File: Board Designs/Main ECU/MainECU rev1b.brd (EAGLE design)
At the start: 121.2 x 79.8 mm, 145 parts, among them X1 CONNECTOR-37, X2 CONNECTOR-4AUTOSPORT, X3 CONNECTOR-4NANO-FIT-VERTICAL-4, X4 CONNECTOR-4NANO-FIT-VERTICAL-4

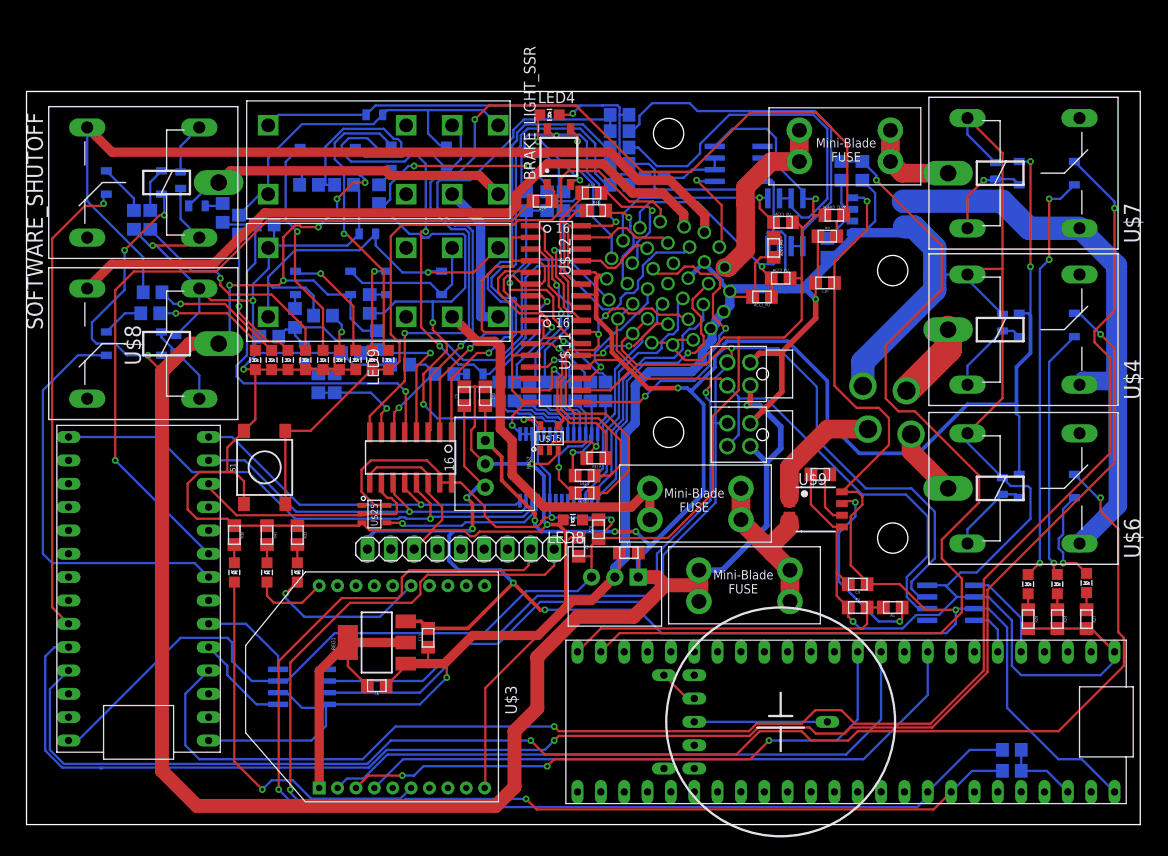
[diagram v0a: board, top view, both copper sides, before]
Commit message: Main ECU rev{1,2}: Update pullup/down resistor informational text, Main ECU rev1b: Update pinout to match Main ECU rev2
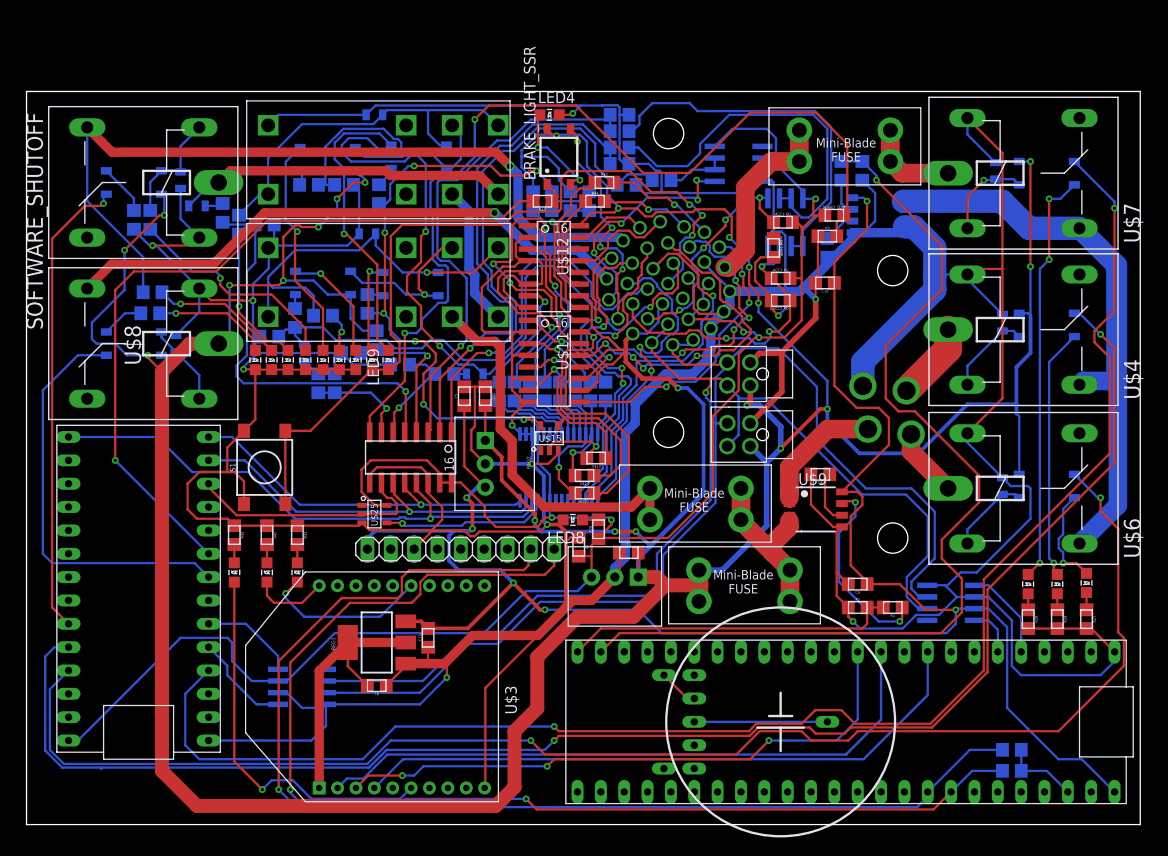
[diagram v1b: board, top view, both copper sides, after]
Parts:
- moved ACC2_PD 2.07 mm to (82.0, 57.0)
- moved R43 1.81 mm to (62.9, 69.8)
- moved R44 1.02 mm to (61.8, 67.8)
- moved BR_FILTR 0.80 mm to (69.1, 70.1)
- moved C12 0.76 mm to (65.3, 69.6)
- moved U$16 0.76 mm to (59.2, 67.8)
- moved U$20 0.76 mm to (61.2, 67.8)
- moved U$21 0.76 mm to (55.1, 67.8)
- moved U$22 0.51 mm to (57.1, 67.8)
- moved IMD_LATCH_SSR 0.40 mm to (41.8, 58.8)
- moved R12 0.25 mm to (37.1, 56.6)
- moved U$11 0.23 mm to (57.4, 50.4)
- moved U$12 0.23 mm to (57.4, 60.7)
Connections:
- net +12V: now also X1.P$10, X1.P$34; no longer X1.P$7
- net +5V: now also X1.P$27, X1.P$28, X1.P$29; no longer X1.P$11, X1.P$12, X1.P$13
- net BMS_OK: now also X1.P$31; no longer X1.P$19
- net BRAKE_LIGHT: now also X1.P$9; no longer X1.P$6
- net CANH: now also X1.P$12, X1.P$13; no longer X1.P$10, X1.P$25
- net CANL: now also X1.P$11, X1.P$26; no longer X1.P$24, X1.P$9
- net DASH_CTRL10: now also X1.P$32; no longer X1.P$28
- net DASH_CTRL11: now also X1.P$6; no longer X1.P$35
- net DASH_CTRL12: now also X1.P$22; no longer X1.P$34
- net DASH_CTRL9: now also X1.P$23; no longer X1.P$29
- net DASH_IO1: now also X1.P$1; no longer X1.P$22
- net DASH_IO2: now also X1.P$2; no longer X1.P$23
- net DASH_IO3: now also X1.P$3; no longer X1.P$21
- net DASH_IO4: now also X1.P$4; no longer X1.P$20
- net DASH_IO5: now also X1.P$18; no longer X1.P$32
- net DASH_IO6: now also X1.P$19; no longer X1.P$33
- net DASH_IO7: now also X1.P$20; no longer X1.P$26
- net DASH_IO8: now also X1.P$21; no longer X1.P$27
- net INVERTER_SUPPLY: now also X1.P$7; no longer X1.P$2
- net LATCH_EXT_BUTTON: now also X1.P$37; no longer X1.P$3
- net OKHS: now also X1.P$33; no longer X1.P$8
- net SHUTDOWN_D: now also X1.P$5; no longer X1.P$1
- net SIGNAL_ACCEL1: now also X1.P$25; no longer X1.P$5
- net SIGNAL_ACCEL2: now also X1.P$24; no longer X1.P$4
- net SIGNAL_BRAKE: now also X1.P$8; no longer X1.P$18
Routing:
- net +12V: track 461.3 -> 487.5 mm, vias 17 -> 22
- net DASH_IO6: track 35.0 -> 61.0 mm, vias 1 -> 5
- net DASH_IO7: track 32.7 -> 57.9 mm, vias 2 -> 4
- net SIGNAL_BRAKE: track 10.5 -> 26.0 mm, vias 1 -> 4
- net +5V: track 299.8 -> 286.8 mm, vias 8 -> 12
- net LATCH_EXT_BUTTON: track 75.0 -> 87.8 mm, vias 0 -> 3
- net DASH_CTRL10: track 28.6 -> 40.7 mm, vias 0 -> 1
- net INVERTER_SUPPLY: track 74.9 -> 62.9 mm, vias 0 -> 1
- net DASH_CTRL12: track 25.1 -> 35.4 mm, vias 0 -> 3
- net BRAKE_LIGHT: track 15.9 -> 25.3 mm, vias 1 -> 4
- net CANH: track 134.2 -> 125.5 mm, vias 1 -> 0
- net OKHS: track 50.5 -> 57.7 mm
- net SHUTDOWN_D: track 93.5 -> 86.6 mm, vias 0 -> 1
- net DASH_CTRL11: track 27.9 -> 34.7 mm, vias 0 -> 1
- net SIGNAL_ACCEL2: track 26.2 -> 32.4 mm, vias 1 -> 3
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
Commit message: Update MainECU rev1b: Update revision silkscreen, Move TLP291-4 (package dimensions incorrect)
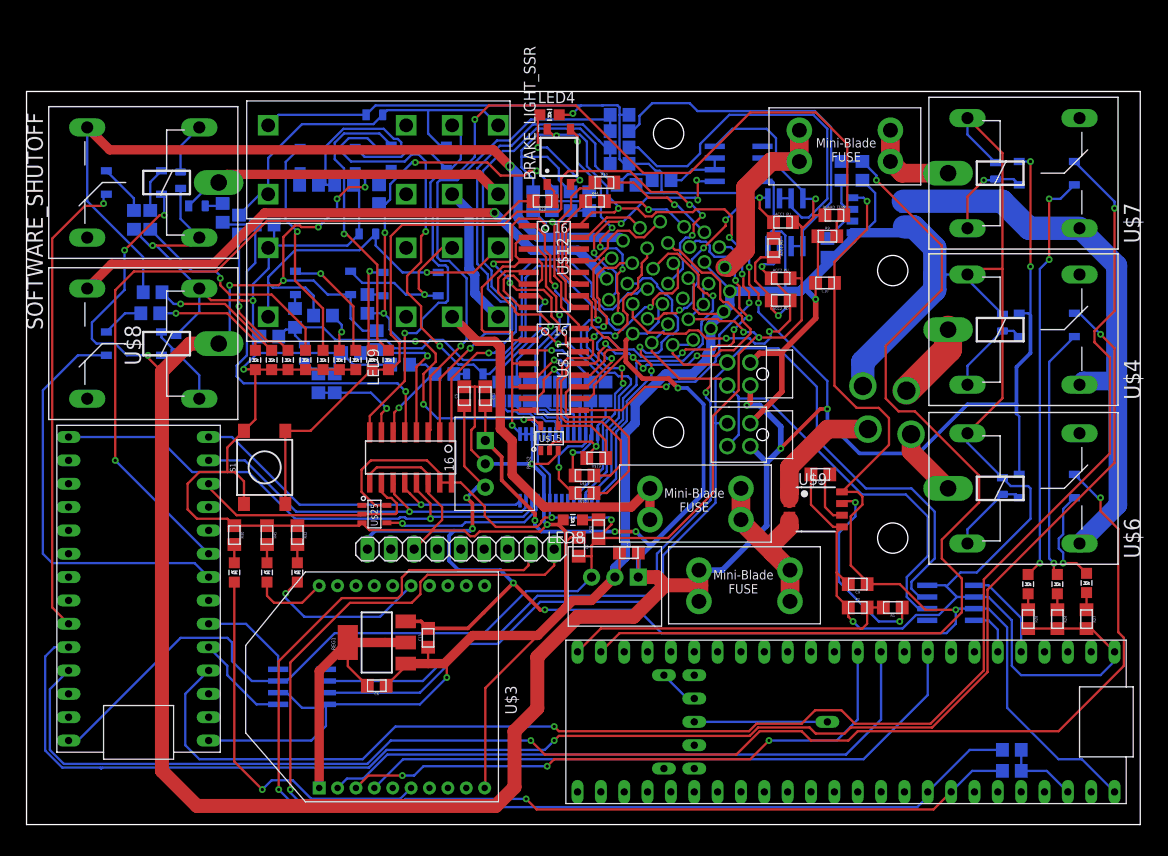
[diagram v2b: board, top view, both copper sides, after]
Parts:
- moved U$11 0.89 mm to (57.4, 49.5)
- flipped U$26 to the bottom, turned to 270 degrees
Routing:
- net +12V: track 487.5 -> 488.8 mm
- net N$55: track 5.39 -> 6.48 mm
- net DASH_IO8: track 37.4 -> 36.4 mm
- net N$62: track 29.5 -> 30.4 mm
- net DASH_IO6: track 61.0 -> 61.7 mm
- net N$61: track 16.7 -> 17.3 mm
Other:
- board text added: "HyTech 2019 Main ECU rev1b"
- board text removed: "HyTech 2019 Main ECU rev1"

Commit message: Library: Update XBee footprint, Add zener diode, toggle TXB010{4,6} value option; MainECU rev1b: add SPI level shifter, switch to separate SPI CS pins, move RTC batt inside board footprint; MainECU rev3: init
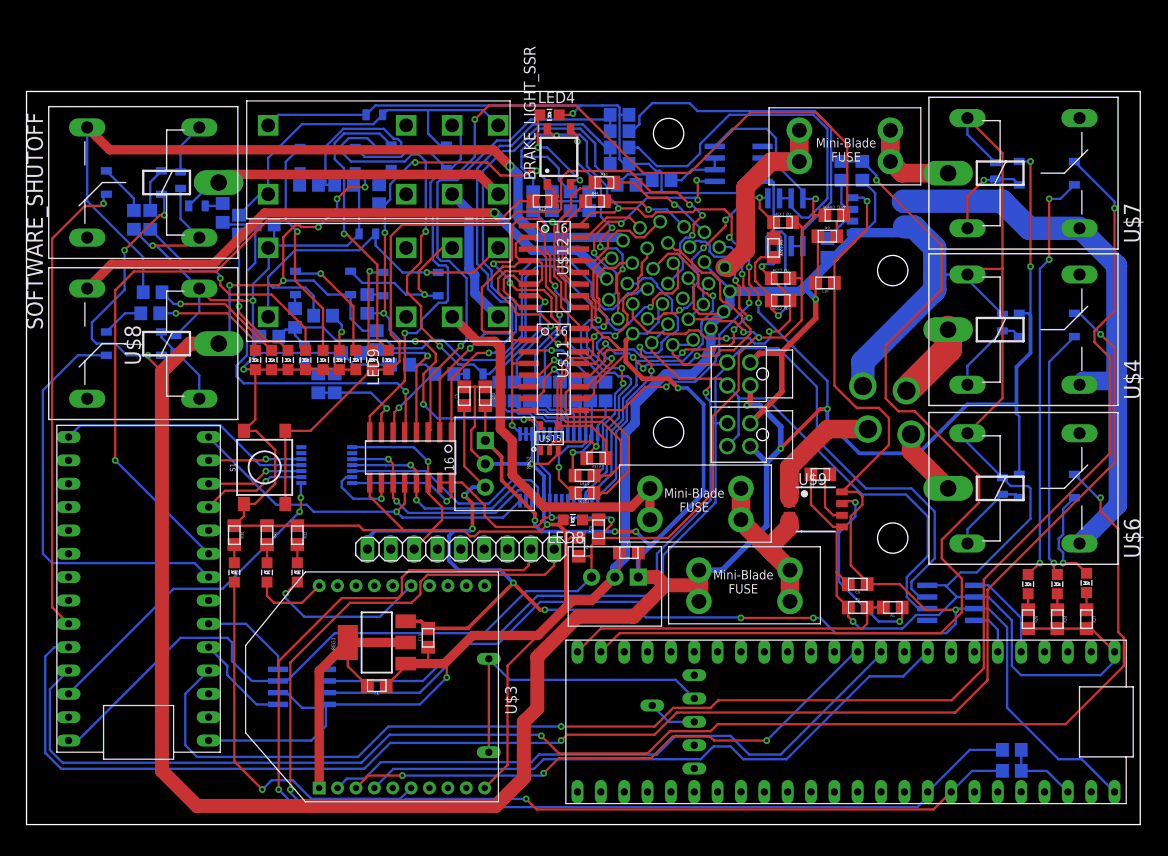
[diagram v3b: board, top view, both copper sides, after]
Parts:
- U$25: value SN74LVC1G06 -> TXB0104TSSOP; device HyTechDevices:SOT-23-5 -> HyTechDevices:TSSOP-14
- moved U$26 19.1 mm to (63.0, 13.0)
- moved U$25 7.54 mm to (32.5, 39.1), flipped to the bottom, turned to 90 degrees
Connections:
- removed net CHIP_SELECT: U$1.D10(TX2), U$18.10, U$25.2
- removed net CHIP_SELECT_INVERTED: U$17.11, U$25.4
- new net 3.3V_MAIN_TEENSY: U$1.3.3V, U$25.1
- new net CS1_5V: U$18.10, U$25.13
- new net CS1_TEENSY: U$1.D9(RX2), U$25.2
- new net CS2_5V: U$17.11, U$25.12
- new net CS2_TEENSY: U$1.D10(TX2), U$25.3
- new net MOSI_5V: U$17.13, U$18.11, U$25.10
- new net N$65: U$25.7
- new net SCK_5V: U$17.12, U$18.13, U$25.11
- net +5V: now also U$25.14; no longer U$25.5
- net GND: now also U$25.8; no longer U$25.3
- net MOSI_TEENSY: now also U$25.5; no longer U$17.13, U$18.11
- net SCK_TEENSY: now also U$25.4; no longer U$17.12, U$18.13
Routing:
- net 3.3V_MAIN_TEENSY: track 0.00 -> 36.5 mm, vias 0 -> 2
- net SCK_TEENSY: track 60.1 -> 27.6 mm, vias 1 -> 0
- net MOSI_TEENSY: track 41.7 -> 10.1 mm
- net N$41: track 4.35 -> 34.3 mm
- net CHIP_SELECT: track 26.4 -> 0.00 mm
- net SCK_5V: track 0.00 -> 25.9 mm, vias 0 -> 2
- net MOSI_5V: track 0.00 -> 25.6 mm, vias 0 -> 2
- net CS2_5V: track 0.00 -> 24.5 mm
- net CHIP_SELECT_INVERTED: track 18.2 -> 0.00 mm, vias 1 -> 0
- net CS1_TEENSY: track 0.00 -> 11.4 mm, vias 0 -> 1
- net CS2_TEENSY: track 0.00 -> 10.7 mm, vias 0 -> 1
- net N$64: track 14.5 -> 5.31 mm
- net CS1_5V: track 0.00 -> 8.56 mm, vias 0 -> 1
- net XBDI: track 65.0 -> 61.1 mm
- net +5V: track 287.1 -> 284.2 mm, vias 12 -> 13
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
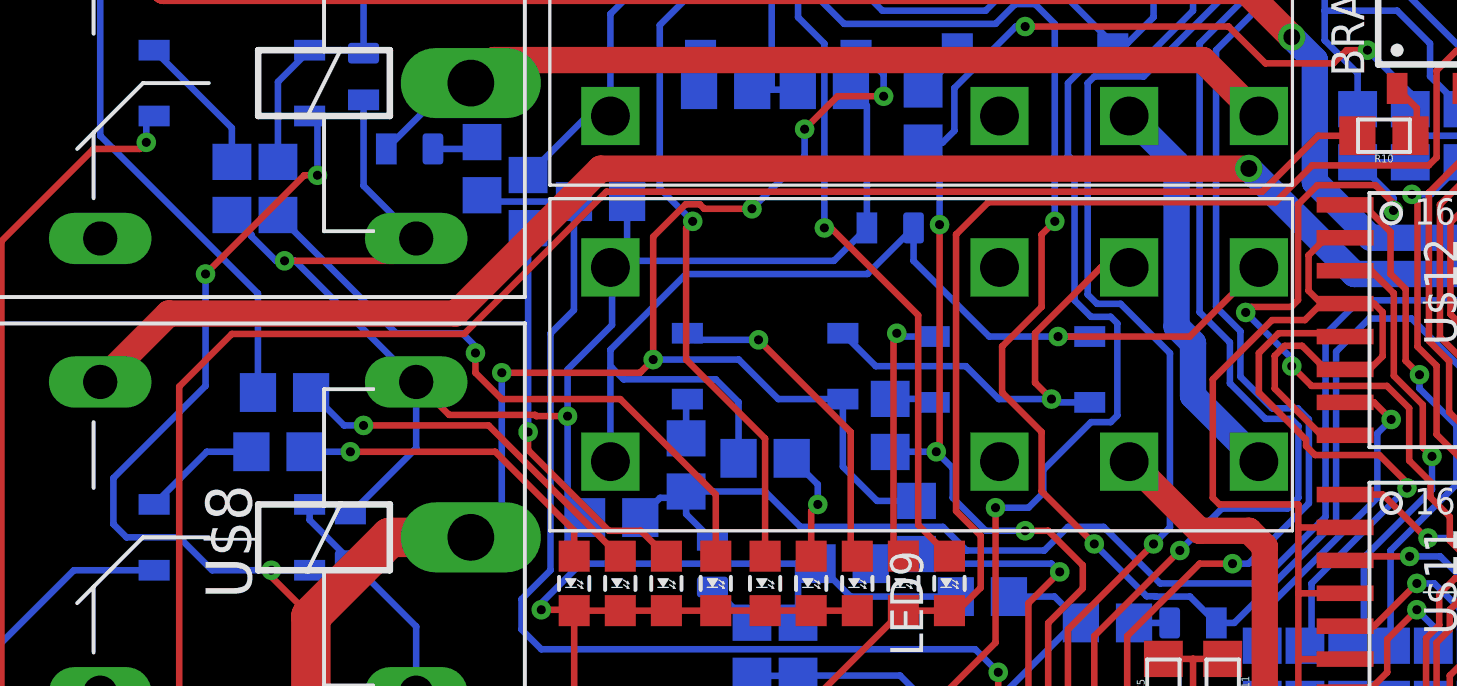
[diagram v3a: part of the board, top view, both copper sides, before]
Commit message: Main ECU: [rev2, rev3] Fix filter frequency capacitor values, [rev1b, rev3] shorten a few traces
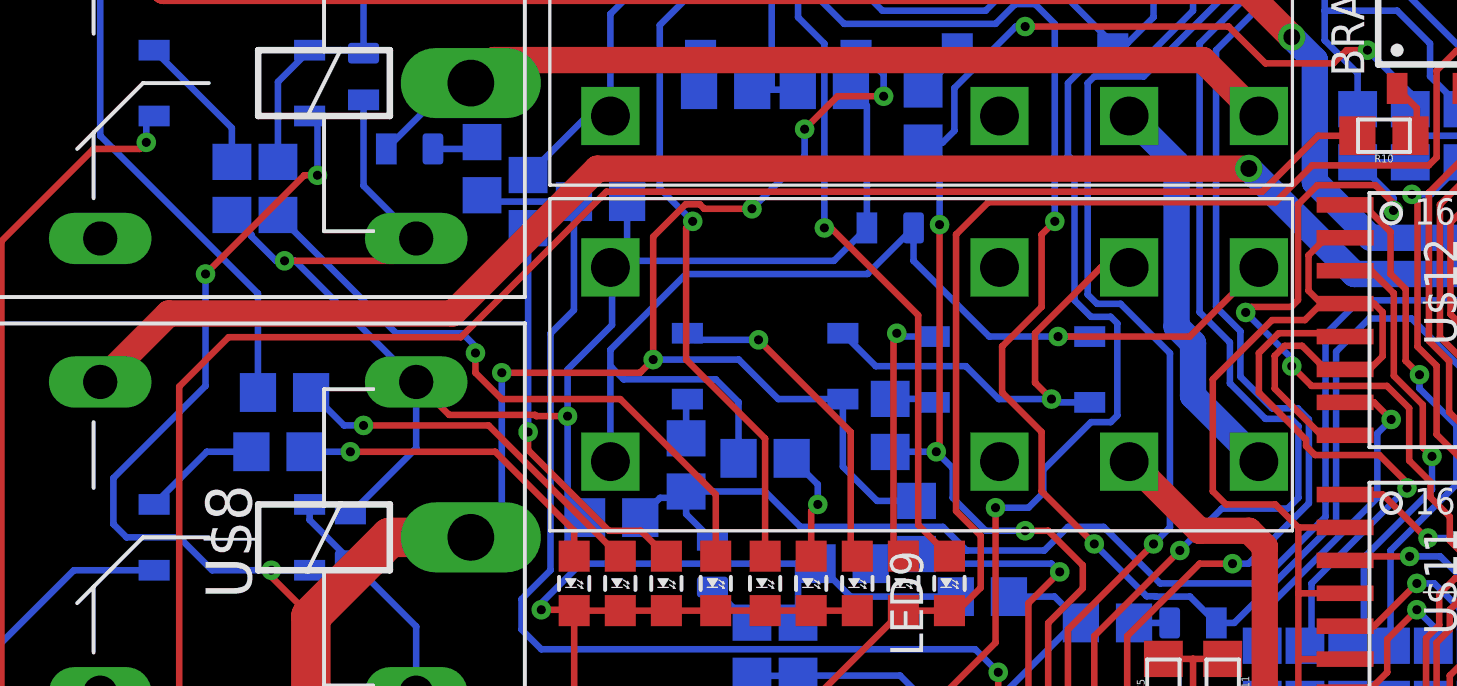
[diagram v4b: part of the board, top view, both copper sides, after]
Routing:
- net GND: track 767.6 -> 767.0 mm
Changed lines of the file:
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@@
 <wire x1="24.892" y1="44.071" x2="24.892" y2="49.496" width="0.254" layer="1"/>
 <wire x1="52.832" y1="50.165" x2="52.832" y2="52.705" width="0.254" layer="1"/>
-<wire x1="52.832" y1="52.705" x2="52.832" y2="53.594" width="0.254" layer="1"/>
 <wire x1="52.832" y1="47.625" x2="52.832" y2="50.165" width="0.254" layer="1"/>
 <wire x1="36.184" y1="64.262" x2="34.914" y2="62.992" width="0.254" layer="16"/>
@@
 <wire x1="56.0832" y1="61.0108" x2="56.0832" y2="59.309" width="0.254" layer="1"/>
 <wire x1="55.753" y1="61.341" x2="56.0832" y2="61.0108" width="0.254" layer="1"/>
-<wire x1="52.832" y1="53.594" x2="49.784" y2="53.594" width="0.254" layer="1"/>
-<wire x1="49.784" y1="53.594" x2="49.53" y2="53.848" width="0.254" layer="1"/>
-<wire x1="49.53" y1="53.848" x2="49.53" y2="58.42" width="0.254" layer="1"/>
 <wire x1="54.6354" y1="56.261" x2="53.721" y2="56.261" width="0.254" layer="1"/>
 <wire x1="51.9204" y1="59.3273875" x2="52.3056125" y2="59.7126" width="0.254" layer="1"/>
@@
 <wire x1="43.688" y1="36.068" x2="43.688" y2="37.211" width="0.254" layer="1"/>
 <wire x1="43.688" y1="37.211" x2="43.688" y2="39.497" width="0.254" layer="1"/>
+<wire x1="52.832" y1="52.705" x2="51.943" y2="53.594" width="0.254" layer="1"/>
+<wire x1="51.943" y1="53.594" x2="50.038" y2="53.594" width="0.254" layer="1"/>
+<wire x1="50.038" y1="53.594" x2="49.53" y2="54.102" width="0.254" layer="1"/>
+<wire x1="49.53" y1="54.102" x2="49.53" y2="58.42" width="0.254" layer="1"/>
 </signal>
 <signal name="+12V">
@@
 <contactref element="U$8" pad="S"/>
 <wire x1="6.604" y1="58.3184" x2="9.2456" y2="60.96" width="1.016" layer="1"/>
-<wire x1="9.2456" y1="60.96" x2="20.32" y2="60.96" width="1.016" layer="1"/>
-<wire x1="20.32" y1="60.96" x2="25.908" y2="66.548" width="1.016" layer="1"/>
-<wire x1="25.908" y1="66.548" x2="50.927" y2="66.548" width="1.016" layer="1"/>
+<wire x1="9.2456" y1="60.96" x2="20.193" y2="60.96" width="1.016" layer="1"/>
+<wire x1="20.193" y1="60.96" x2="25.781" y2="66.548" width="1.016" layer="1"/>
+<wire x1="25.781" y1="66.548" x2="50.927" y2="66.548" width="1.016" layer="1"/>
 <contactref element="X1" pad="P$7"/>
 <wire x1="50.927" y1="66.548" x2="50.918871875" y2="66.556128125" width="0.254" layer="1"/>
@@
 <contactref element="R10" pad="2"/>
 <contactref element="U$1" pad="D7(RX3)"/>
-<wire x1="20.64615625" y1="60.1726" x2="11.684" y2="60.1726" width="0.254" layer="1"/>
-<wire x1="26.13255625" y1="65.659" x2="20.64615625" y2="60.1726" width="0.254" layer="1"/>
-<wire x1="11.684" y1="60.1726" x2="9.652" y2="58.1406" width="0.254" layer="1"/>
+<wire x1="20.51915625" y1="60.0456" x2="11.557" y2="60.0456" width="0.254" layer="1"/>
+<wire x1="26.13255625" y1="65.659" x2="20.51915625" y2="60.0456" width="0.254" layer="1"/>
+<wire x1="11.557" y1="60.0456" x2="9.652" y2="58.1406" width="0.254" layer="1"/>
 <via x="9.652" y="39.624" extent="1-16" drill="0.35"/>
 <wire x1="9.652" y1="39.624" x2="19.812" y2="29.464" width="0.254" layer="16"/>
